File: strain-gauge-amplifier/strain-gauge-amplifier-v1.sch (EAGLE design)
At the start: 25 parts, among them IC2 INA125U, M1 #4-BARE_MOUNTING_HOLE/.300, M2 #4-BARE_MOUNTING_HOLE/.300, M3 #4-BARE_MOUNTING_HOLE/.300, M4 #4-BARE_MOUNTING_HOLE/.300, Q1 PMV45EN

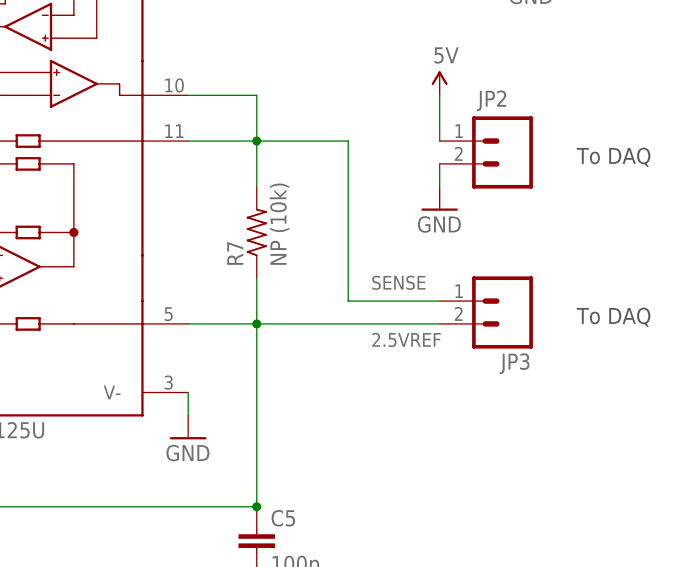
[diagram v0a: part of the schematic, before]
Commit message: Cleaned up board a bit - mostly made things wider, cleaned up one part placement.
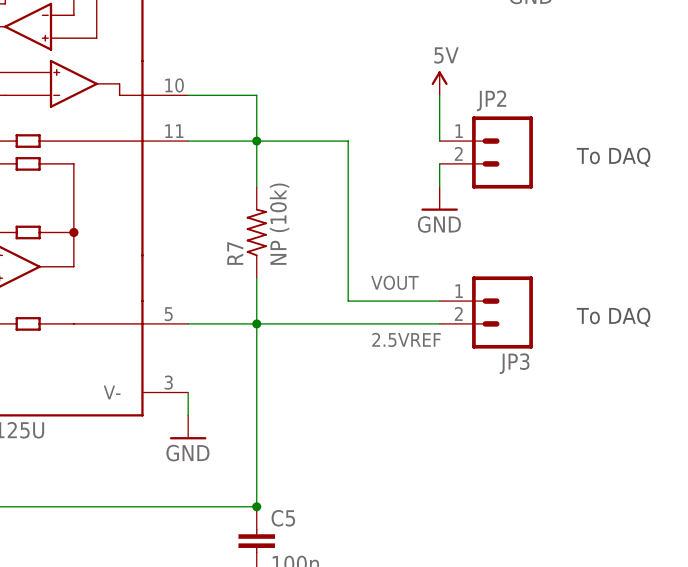
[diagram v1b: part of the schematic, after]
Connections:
- net SENSE renamed VOUT
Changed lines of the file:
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@@
 <?xml version="1.0" encoding="utf-8"?>
 <!DOCTYPE eagle SYSTEM "eagle.dtd">
-<eagle version="6.4">
+<eagle version="6.5.0">
 <drawing>
 <settings>
@@
 <setting verticaltext="up"/>
 </settings>
-<grid distance="0.01" unitdist="inch" unit="inch" style="dots" multiple="1" display="yes" altdistance="0.001" altunitdist="inch" altunit="inch"/>
+<grid distance="0.1" unitdist="inch" unit="inch" style="lines" multiple="1" display="no" altdistance="0.01" altunitdist="inch" altunit="inch"/>
 <layers>
 <layer number="1" name="Top" color="4" fill="1" visible="no" active="no"/>
@@
 </segment>
 </net>
-<net name="SENSE" class="0">
+<net name="VOUT" class="0">
 <segment>
 <pinref part="IC2" gate="G$1" pin="OUT"/>

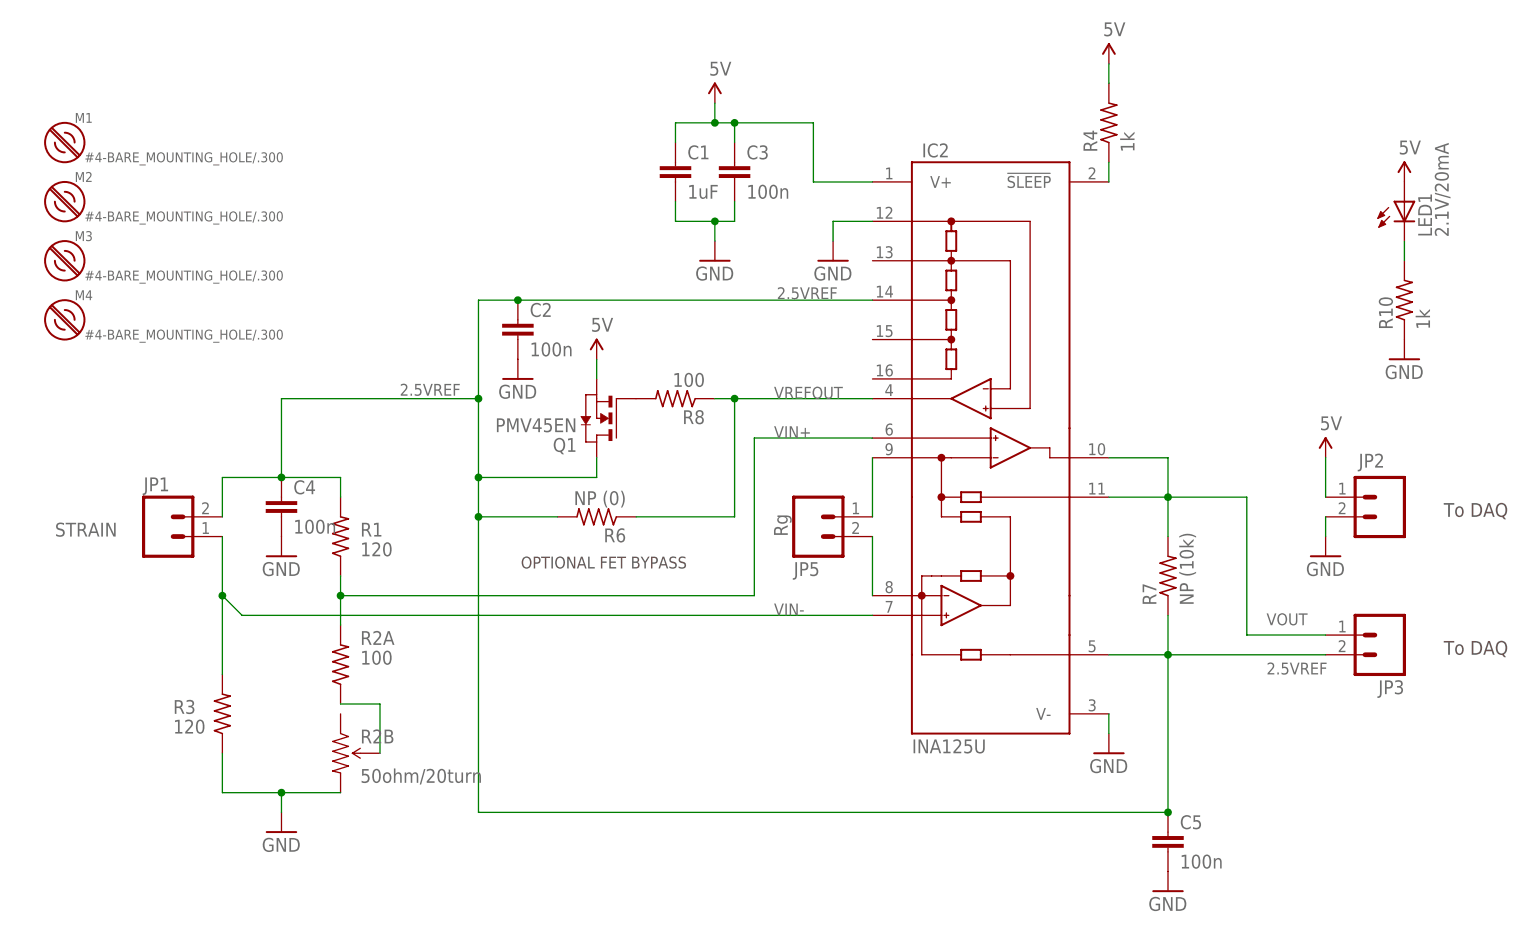
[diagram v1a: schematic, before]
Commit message: Changed trim pot footprint; had to change layout.
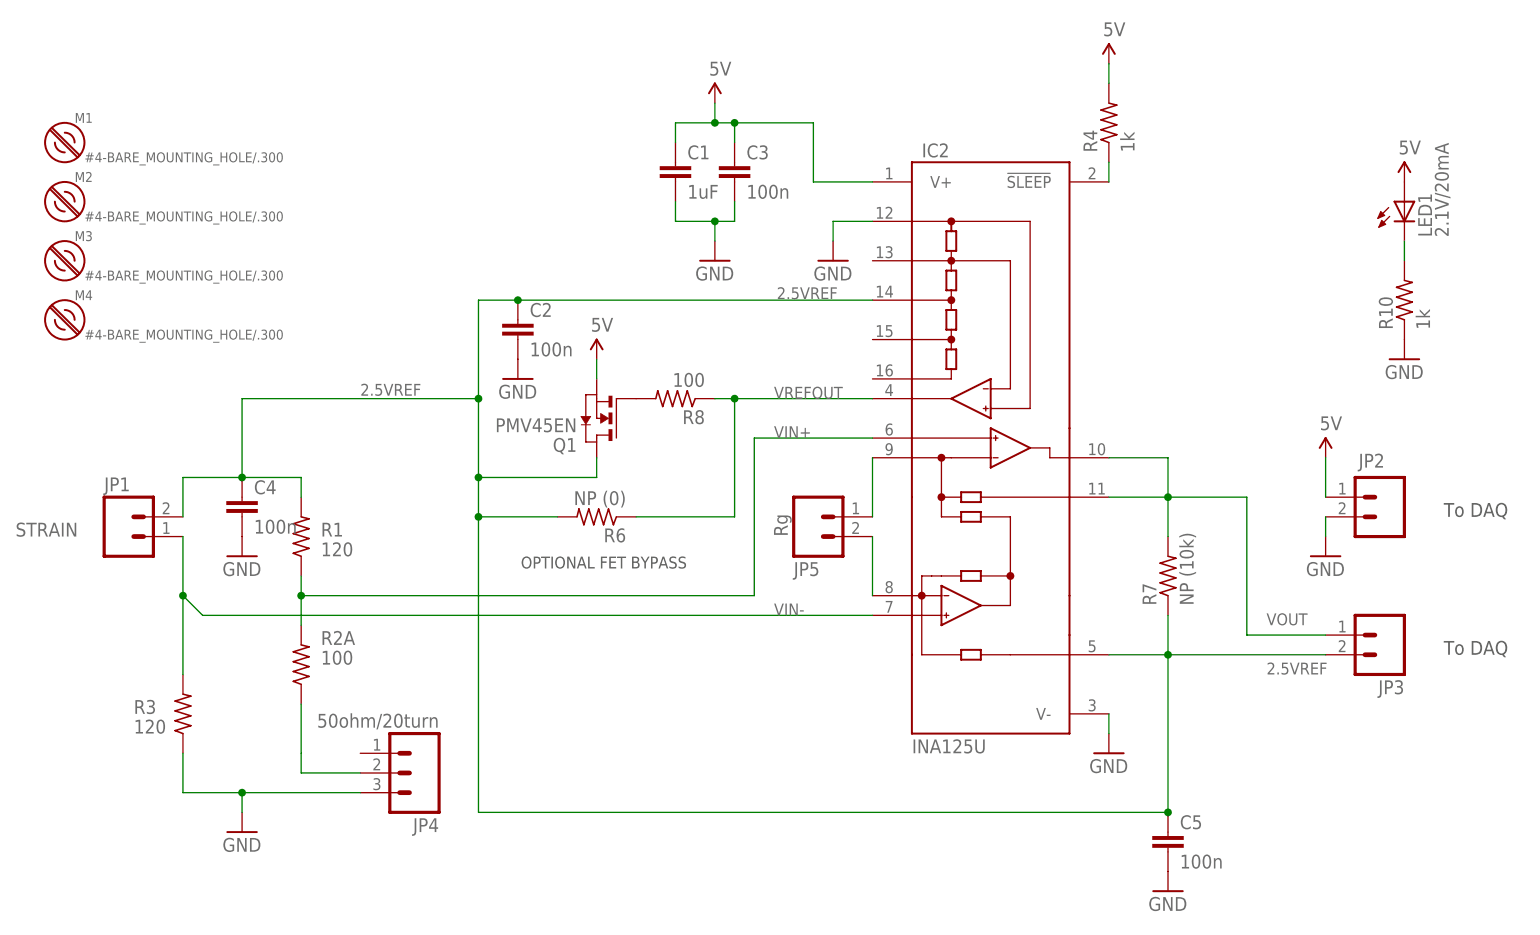
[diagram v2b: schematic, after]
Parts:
- removed R2B: 50ohm/20turn, SparkFun-Electromechanical:TRIMPOTTRIMPOT-5MM
- added JP4: 50ohm/20turn, SparkFun-Connectors:M031X03_NO_SILK
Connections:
- net GND: now also JP4.3; no longer R2B.CW
- net N$1: now also JP4.2; no longer R2B.WIPER
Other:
- moved on the sheet: C4, JP1, R1, R2A, R3
